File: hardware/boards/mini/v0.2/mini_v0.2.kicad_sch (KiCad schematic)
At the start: 99 parts, among them IC1 NAU88C22YG, IC3 IS42S16160J-6BLI, J2 Top, J3 Bottom, Q1 PMV37EN22, U1 W25Q128JVP, U2 LTV-217-G, U4 STM32H750XBHx, Y1 Crystal_GND24, Y3 32.768kHz

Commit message: mini: fix mounting bite sizing, make power input reversable without damage
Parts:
- C1, C2, C3: LCSC (none) -> C170151
- C15: value R -> C
- C34, C35, C69: LCSC (none) -> C315248
- C4: LCSC (none) -> C14445
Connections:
- net +3.3V: no longer J2.51
- net AUX_IN_L: now also J2.28; no longer J2.26
- net AUX_IN_R: now also J2.26; no longer J2.24
- net PA11/4RX: now also J2.5; no longer J2.1
- net PA12/4TX: now also J2.7; no longer J2.3
- net SDMMC1_CK: now also J2.20; no longer J2.18
- net SDMMC1_CMD: now also J2.22; no longer J2.20
- net SDMMC1_D0: now also J2.12; no longer J2.10
- net SDMMC1_D1: now also J2.14; no longer J2.12
- net SDMMC1_D2: now also J2.16; no longer J2.14
- net SDMMC1_D3: now also J2.18; no longer J2.16
- net SPI_NSS: now reaches J2.8
- net SPI_NSS: now also U4.A16 (PI0)
- net PH15: no longer names the net of U4.B16 (PH15)
- net PH15: no longer J2.7
- removed net PI0: J2.5, U4.A16 (PI0)
- no-connect marks 1 -> 3
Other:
- note added: "1 and 3 are NC to prevent damage if the module is reversed in the sockets."

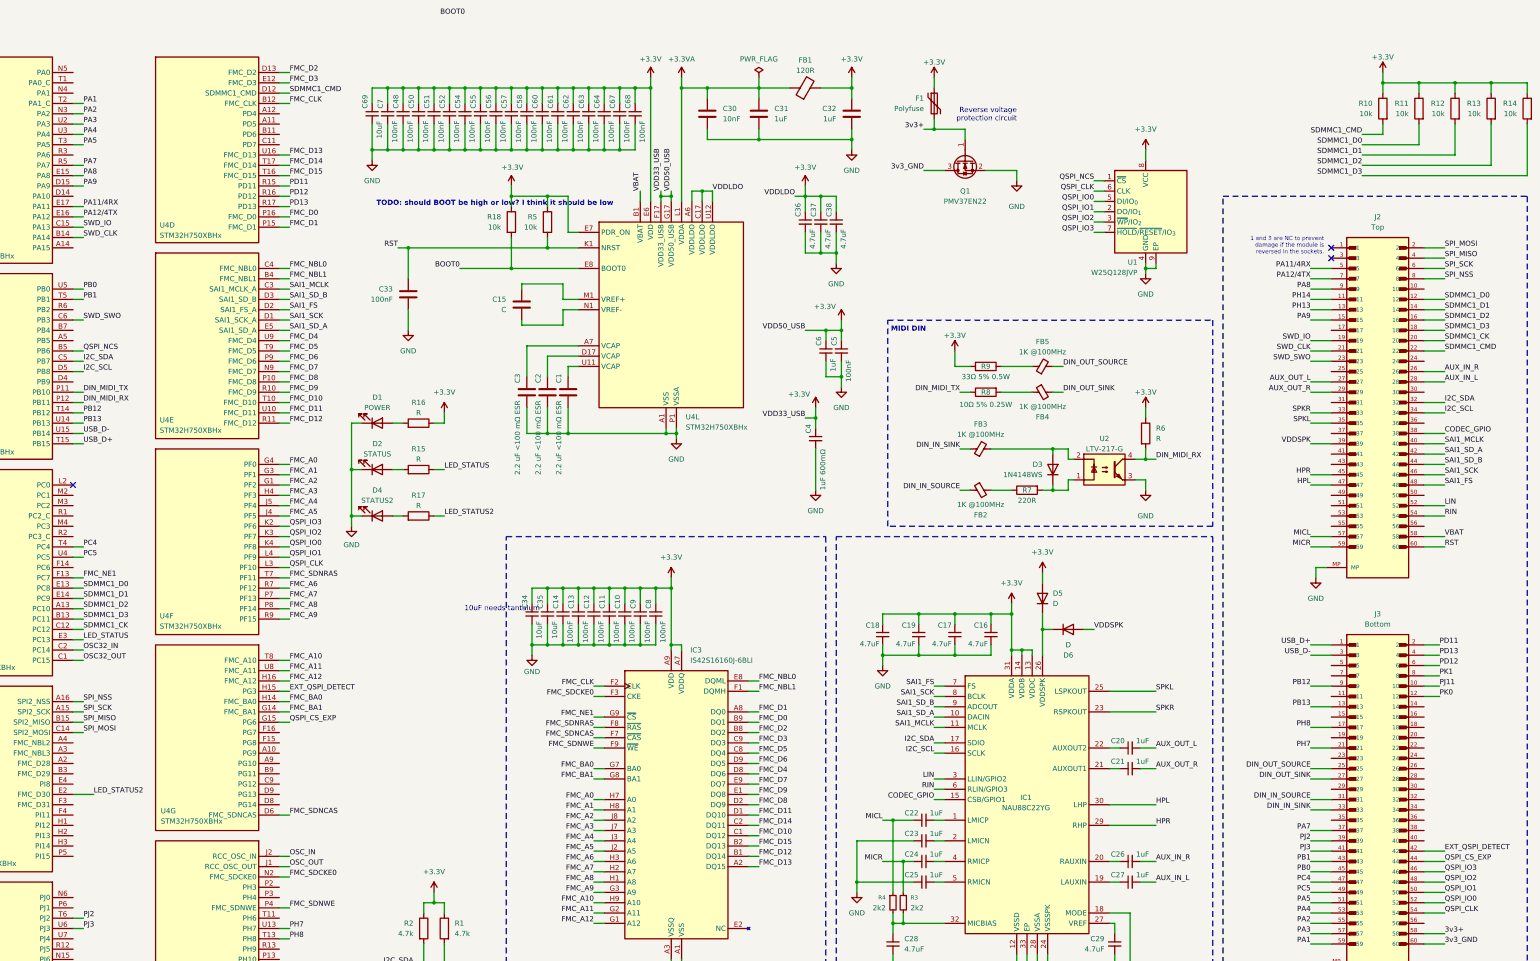
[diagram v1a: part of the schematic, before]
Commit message: mini: start routing remaining lower GPIO
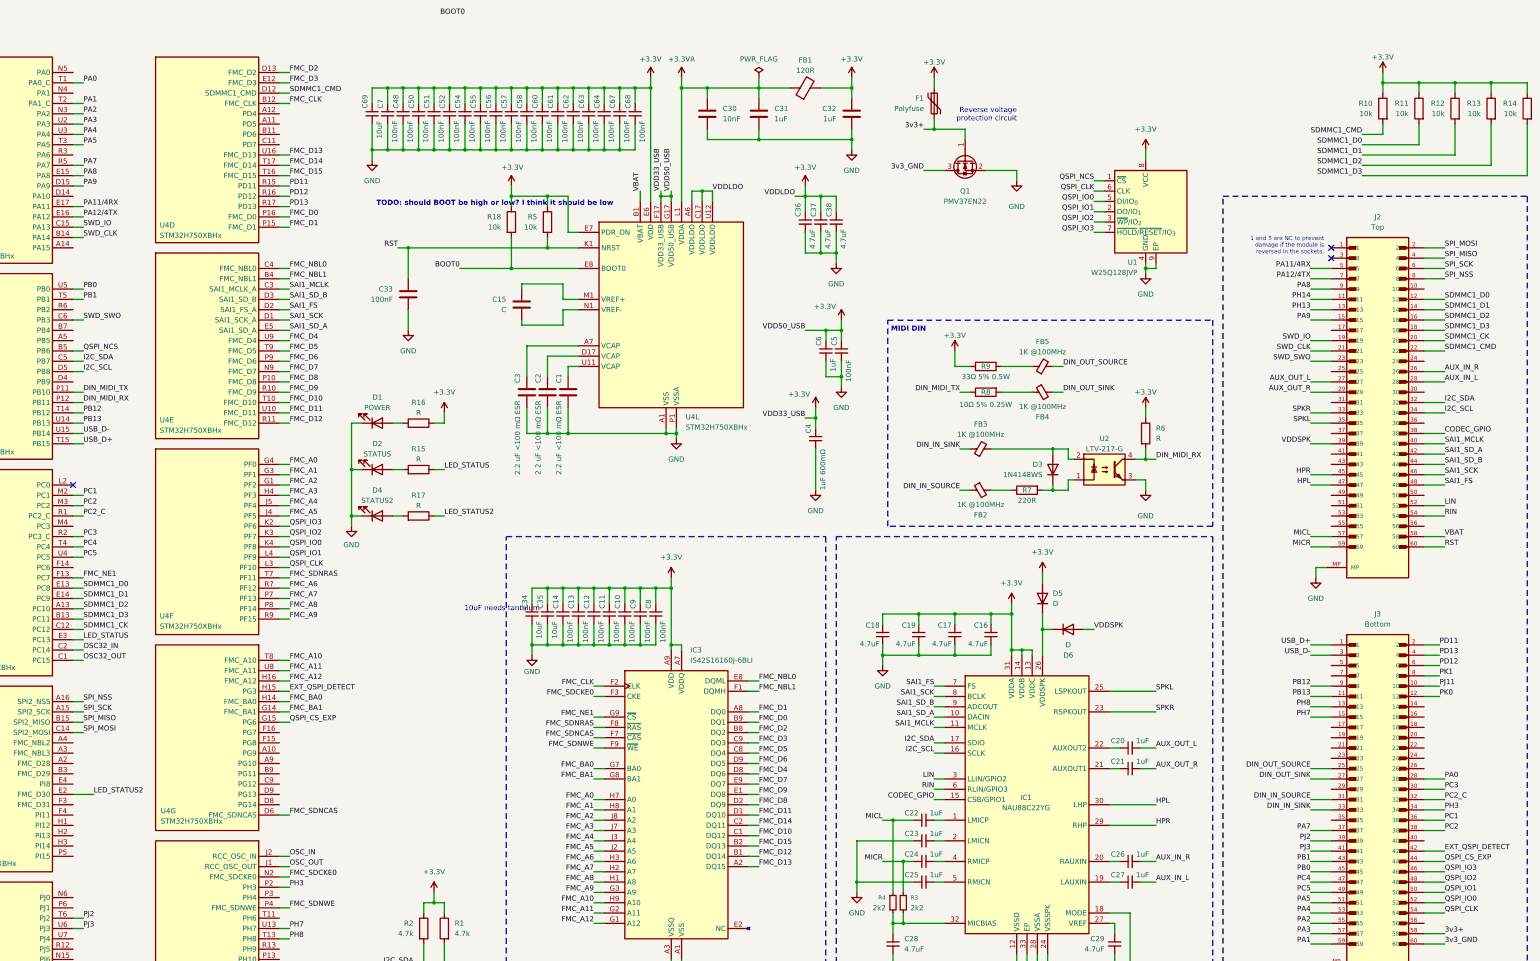
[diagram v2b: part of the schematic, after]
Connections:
- net PB13: now also J3.11; no longer J3.13
- net PH7: now also J3.15; no longer J3.21
- net PH8: now also J3.13; no longer J3.17
- net PH3: now reaches U4.P2 (PH3)
- net PH3: now also J3.34
- net PA0: now reaches U4.T1 (PA0_C)
- net PA0: now also J3.28
- net PC1: now reaches U4.M2 (PC1)
- net PC1: now also J3.36
- net PC2: now reaches U4.M3 (PC2)
- net PC2: now also J3.38
- net PC2_C: now reaches U4.R1 (PC2_C)
- net PC2_C: now also J3.32
- net PC3: now reaches U4.R2 (PC3_C)
- net PC3: now also J3.30
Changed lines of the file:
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@@
 	(wire
 		(pts
+			(xy 96.52 219.71) (xy 99.06 219.71)
+		)
+		(stroke
+			(width 0)
+			(type default)
+		)
+	)
+	(wire
+		(pts
 			(xy 99.06 166.37) (xy 96.52 166.37)
 		)
@@
 	(wire
 		(pts
+			(xy 45.72 125.73) (xy 48.26 125.73)
+		)
+		(stroke
+			(width 0)
+			(type default)
+		)
+	)
+	(wire
+		(pts
 			(xy 212.09 194.31) (xy 214.63 194.31)
 		)
@@
 	(wire
 		(pts
+			(xy 45.72 123.19) (xy 48.26 123.19)
+		)
+		(stroke
+			(width 0)
+			(type default)
+		)
+	)
+	(wire
+		(pts
 			(xy 284.48 156.21) (xy 284.48 162.56)
 		)
@@
 	(wire
 		(pts
+			(xy 378.46 195.58) (xy 383.54 195.58)
+		)
+		(stroke
+			(width 0)
+			(type default)
+		)
+	)
+	(wire
+		(pts
 			(xy 215.9 260.35) (xy 231.14 260.35)
 		)
@@
 	(wire
 		(pts
+			(xy 45.72 21.59) (xy 48.26 21.59)
+		)
+		(stroke
+			(width 0)
+			(type default)
+		)
+	)
+	(wire
+		(pts
 			(xy 194.31 238.76) (xy 194.31 240.03)
 		)
@@
 	(wire
 		(pts
-			(xy 350.52 175.26) (xy 355.6 175.26)
+			(xy 350.52 172.72) (xy 355.6 172.72)
 		)
 		(stroke
@@
 	(wire
 		(pts
+			(xy 378.46 193.04) (xy 383.54 193.04)
+		)
+		(stroke
+			(width 0)
+			(type default)
+		)
+	)
+	(wire
+		(pts
 			(xy 378.46 62.23) (xy 383.54 62.23)
 		)
@@
 	(wire
 		(pts
+			(xy 378.46 205.74) (xy 383.54 205.74)
+		)
+		(stroke
+			(width 0)
+			(type default)
+		)
+	)
+	(wire
+		(pts
 			(xy 96.52 140.97) (xy 99.06 140.97)
 		)
@@
 	(wire
 		(pts
+			(xy 378.46 198.12) (xy 383.54 198.12)
+		)
+		(stroke
+			(width 0)
+			(type default)
+		)
+	)
+	(wire
+		(pts
 			(xy 237.49 22.86) (xy 237.49 25.4)
 		)
@@
 	(wire
 		(pts
+			(xy 45.72 128.27) (xy 48.26 128.27)
+		)
+		(stroke
+			(width 0)
+			(type default)
+		)
+	)
+	(wire
+		(pts
 			(xy 45.72 54.61) (xy 48.26 54.61)
 		)
@@
 	(wire
 		(pts
+			(xy 378.46 200.66) (xy 383.54 200.66)
+		)
+		(stroke
+			(width 0)
+			(type default)
+		)
+	)
+	(wire
+		(pts
 			(xy 127 105.41) (xy 124.46 105.41)
 		)
@@
 	(wire
 		(pts
+			(xy 378.46 203.2) (xy 383.54 203.2)
+		)
+		(stroke
+			(width 0)
+			(type default)
+		)
+	)
+	(wire
+		(pts
 			(xy 363.22 39.37) (xy 386.08 39.37)
 		)
@@
 	(wire
 		(pts
+			(xy 45.72 133.35) (xy 48.26 133.35)
+		)
+		(stroke
+			(width 0)
+			(type default)
+		)
+	)
+	(wire
+		(pts
 			(xy 350.52 120.65) (xy 355.6 120.65)
 		)
@@
 	(wire
 		(pts
-			(xy 350.52 185.42) (xy 355.6 185.42)
+			(xy 350.52 177.8) (xy 355.6 177.8)
 		)
 		(stroke
@@
 	(wire
 		(pts
-			(xy 350.52 180.34) (xy 355.6 180.34)
+			(xy 350.52 175.26) (xy 355.6 175.26)
 		)
 		(stroke
@@
 	)
 	(label "PH8"
-		(at 350.52 180.34 180)
+		(at 350.52 175.26 180)
 		(effects
 			(font
@@
 	)
 	(label "PH7"
-		(at 350.52 185.42 180)
+		(at 350.52 177.8 180)
 		(effects
 			(font
@@
 		)
 	)
+	(label "PH3"
+		(at 383.54 200.66 0)
+		(effects
+			(font
+				(size 1.27 1.27)
+			)
+			(justify left bottom)
+		)
+	)
 	(label "SDMMC1_D1"
 		(at 383.54 77.47 0)
@@
 		)
 	)
+	(label "PA0"
+		(at 48.26 21.59 0)
+		(effects
+			(font
+				(size 1.27 1.27)
+			)
+			(justify left bottom)
+		)
+	)
 	(label "FMC_NBL1"
 		(at 214.63 171.45 0)
@@
 		)
 	)
+	(label "PH3"
+		(at 99.06 219.71 0)
+		(effects
+			(font
+				(size 1.27 1.27)
+			)
+			(justify left bottom)
+		)
+	)
 	(label "FMC_D13"
 		(at 99.06 39.37 0)
@@
 	)
 	(label "PB13"
-		(at 350.52 175.26 180)
+		(at 350.52 172.72 180)
 		(effects
 			(font
@@
 		)
 	)
+	(label "PA0"
+		(at 383.54 193.04 0)
+		(effects
+			(font
+				(size 1.27 1.27)
+			)
+			(justify left bottom)
+		)
+	)
 	(label "FMC_D1"
 		(at 214.63 176.53 0)
@@
 		)
 	)
+	(label "PC3"
+		(at 383.54 195.58 0)
+		(effects
+			(font
+				(size 1.27 1.27)
+			)
+			(justify left bottom)
+		)
+	)
 	(label "PA1"
 		(at 350.52 233.68 180)
@@
 		)
 	)
+	(label "PC2"
+		(at 48.26 125.73 0)
+		(effects
+			(font
+				(size 1.27 1.27)
+			)
+			(justify left bottom)
+		)
+	)
 	(label "QSPI_IO0"
 		(at 99.06 135.89 0)
@@
 		)
 	)
+	(label "PC2"
+		(at 383.54 205.74 0)
+		(effects
+			(font
+				(size 1.27 1.27)
+			)
+			(justify left bottom)
+		)
+	)
 	(label "PD11"
 		(at 99.06 46.99 0)
@@
 		)
 	)
+	(label "PC2_C"
+		(at 383.54 198.12 0)
+		(effects
+			(font
+				(size 1.27 1.27)
+			)
+			(justify left bottom)
+		)
+	)
 	(label "QSPI_CS_EXP"
 		(at 383.54 213.36 0)
@@
 		)
 	)
+	(label "PC1"
+		(at 383.54 203.2 0)
+		(effects
+			(font
+				(size 1.27 1.27)
+			)
+			(justify left bottom)
+		)
+	)
 	(label "PB1"
 		(at 48.26 74.93 0)
@@
 		)
 	)
+	(label "PC3"
+		(at 48.26 133.35 0)
+		(effects
+			(font
+				(size 1.27 1.27)
+			)
+			(justify left bottom)
+		)
+	)
 	(label "SPI_NSS"
 		(at 383.54 69.85 0)
@@
 		)
 	)
+	(label "PC2_C"
+		(at 48.26 128.27 0)
+		(effects
+			(font
+				(size 1.27 1.27)
+			)
+			(justify left bottom)
+		)
+	)
 	(label "FMC_A10"
 		(at 99.06 163.83 0)
@@
 		(effects
 			(font
+				(size 1.27 1.27)
+			)
+			(justify left bottom)
+		)
+	)
+	(label "PC1"
+		(at 48.26 123.19 0)
+		(effects
+			(font
